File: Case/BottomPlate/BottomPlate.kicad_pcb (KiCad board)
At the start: 2 copper layers, 136.5 x 87.7 mm, 8 parts

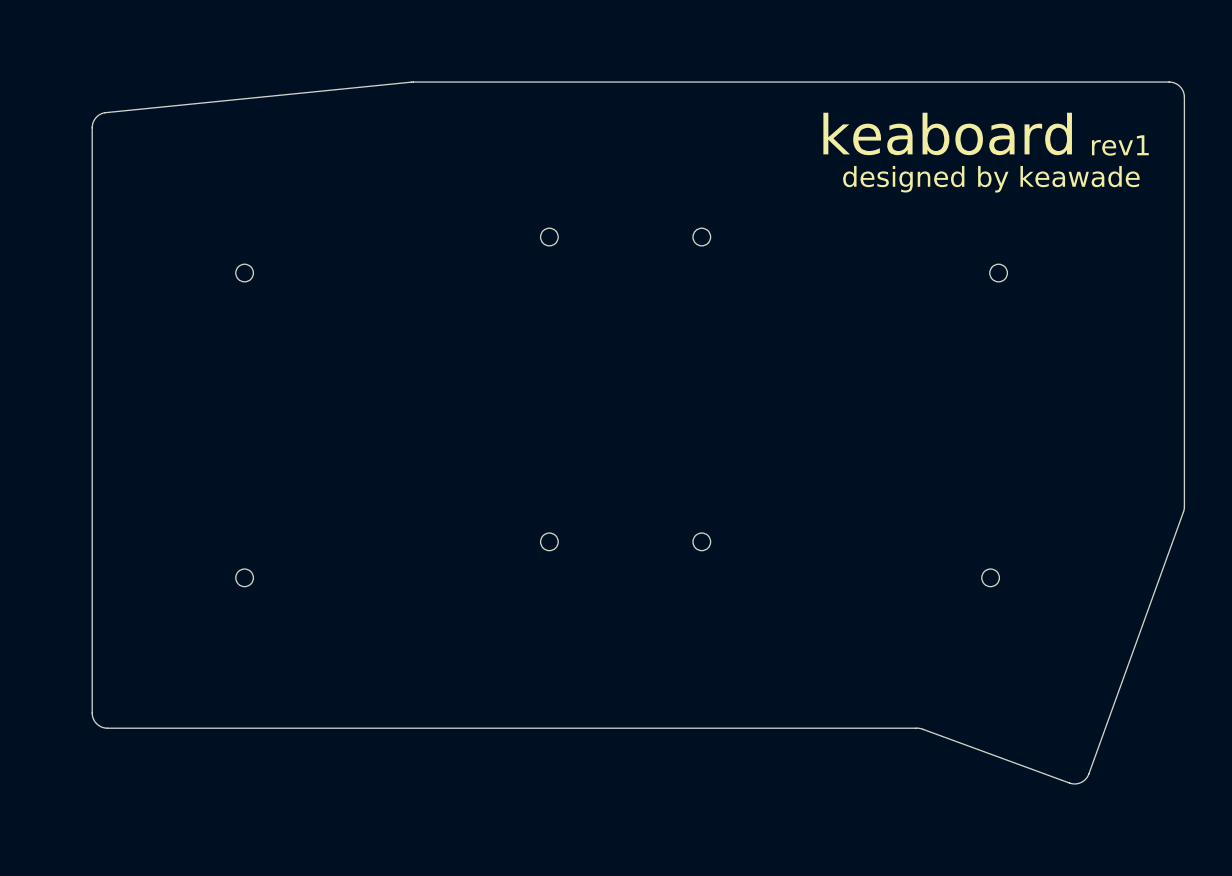
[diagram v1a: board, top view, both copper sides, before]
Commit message: Resize PCB to add more space around the edges to avoid breaking parts, update images, update gerber
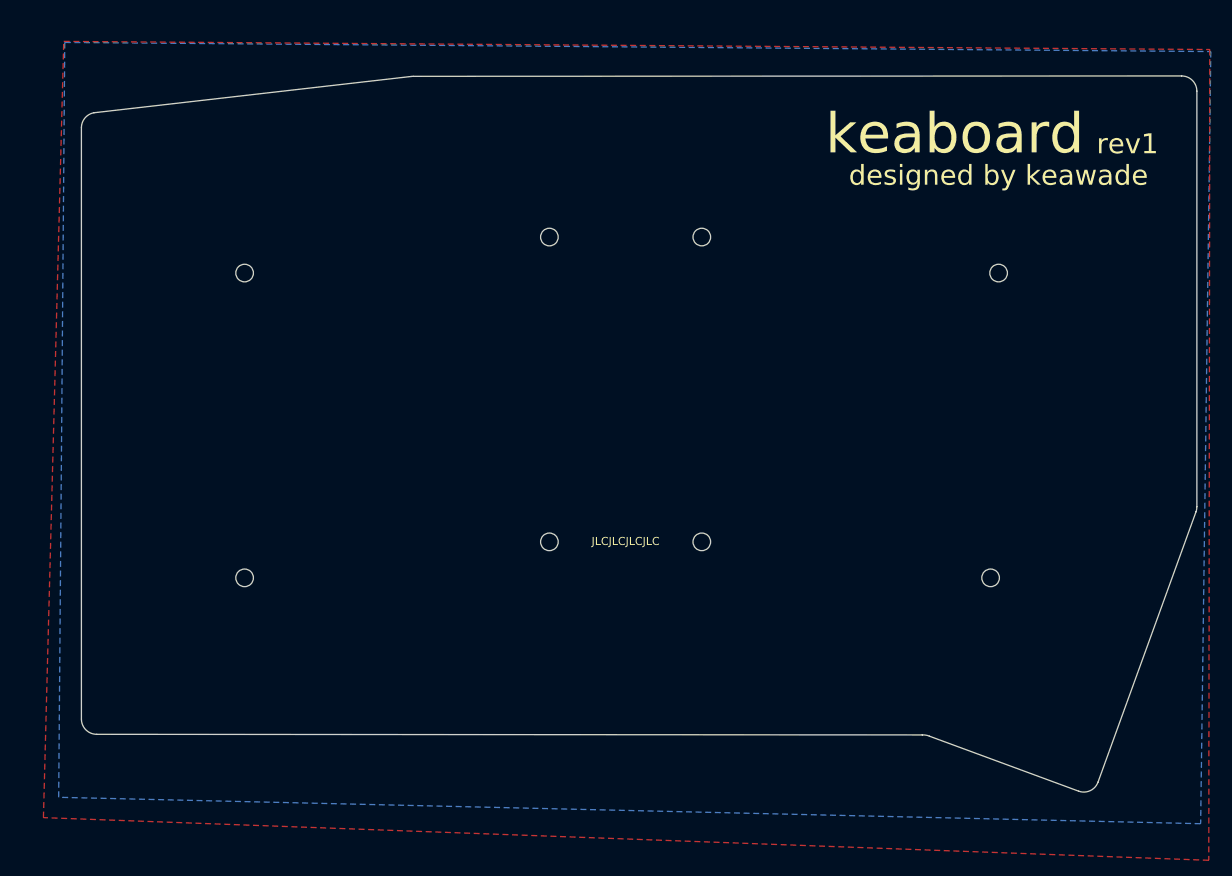
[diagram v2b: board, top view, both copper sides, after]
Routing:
- added copper zone on B.Cu, net (none)
- added copper zone on F.Cu, net (none)
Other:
- board size 136.5 x 87.7 mm -> 139.4 x 89.5 mm
- board text added: "JLCJLCJLCJLC"
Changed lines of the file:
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@@
   (general
     (thickness 1.6)
-    (drawings 20)
+    (drawings 21)
     (tracks 0)
     (zones 0)
@@
     (visible_elements FFFFFF7F)
     (pcbplotparams
-      (layerselection 0x010f0_ffffffff)
+      (layerselection 0x010fc_ffffffff)
       (usegerberextensions false)
       (usegerberattributes true)
@@
     (pad 1 np_thru_hole circle (at 0 0) (size 2.2 2.2) (drill 2.2) (layers *.Cu *.Mask))
   )
-  (gr_text keaboard (at 154.94 58.42) (layer B.SilkS)
+  (gr_text JLCJLCJLCJLC (at 114.681 103.759) (layer F.SilkS)
+    (effects (font (size 1 1) (thickness 0.2)))
+  )
+  (gr_arc (start 88.138 47.546) (end 88.138 45.641) (angle -7.594647344) (layer Edge.Cuts) (width 0.1))
+  (gr_line (start 48.2312 50.193941) (end 87.886228 45.657711) (layer Edge.Cuts) (width 0.1))
+  (gr_line (start 46.657 125.984) (end 46.657 52.07) (layer Edge.Cuts) (width 0.1))
+  (gr_arc (start 151.892001 129.898249) (end 152.654 128.12025) (angle -26.95486857) (layer Edge.Cuts) (width 0.1))
+  (gr_line (start 88.138 45.641) (end 184.186 45.593) (layer Edge.Cuts) (width 0.1))
+  (gr_line (start 185.98101 100.076) (end 173.735996 133.858) (layer Edge.Cuts) (width 0.1))
+  (gr_line (start 151.765273 127.968) (end 48.562 127.889) (layer Edge.Cuts) (width 0.1))
+  (gr_line (start 186.091 47.498) (end 186.091 99.441) (layer Edge.Cuts) (width 0.1))
+  (gr_arc (start 48.562 125.984) (end 46.657 125.984) (angle -90) (layer Edge.Cuts) (width 0.1))
+  (gr_arc (start 48.562 52.07) (end 46.657 52.07) (angle 80) (layer Edge.Cuts) (width 0.1))
+  (gr_arc (start 184.186 47.498) (end 186.091 47.498) (angle -90) (layer Edge.Cuts) (width 0.1))
+  (gr_line (start 171.323 135.001) (end 152.654 128.12025) (layer Edge.Cuts) (width 0.1))
+  (gr_arc (start 184.20301 99.441001) (end 185.98101 100.076) (angle -19.65382589) (layer Edge.Cuts) (width 0.1))
+  (gr_arc (start 171.957998 133.223002) (end 171.323 135.001) (angle -90) (layer Edge.Cuts) (width 0.1))
+  (gr_text keaboard (at 155.829 58.166) (layer B.SilkS)
     (effects (font (size 5 5) (thickness 0.75)) (justify mirror))
   )
-  (gr_text rev1 (at 176.53 57.15) (layer B.SilkS)
+  (gr_text rev1 (at 177.419 56.896) (layer B.SilkS)
     (effects (font (size 2.5 2.5) (thickness 0.4)) (justify mirror))
   )
-  (gr_text "designed by keawade" (at 160.401 53.213) (layer B.SilkS)
+  (gr_text "designed by keawade" (at 161.29 52.959) (layer B.SilkS)
     (effects (font (size 2.5 2.5) (thickness 0.4)) (justify mirror))
   )
-  (gr_text rev1 (at 176.53 54.356) (layer F.SilkS)
+  (gr_text rev1 (at 177.419 54.102) (layer F.SilkS)
     (effects (font (size 2.5 2.5) (thickness 0.4)))
   )
-  (gr_text keaboard (at 154.94 53.086) (layer F.SilkS)
+  (gr_text keaboard (at 155.829 52.832) (layer F.SilkS)
     (effects (font (size 5 5) (thickness 0.75)))
   )
-  (gr_text "designed by keawade" (at 160.401 58.293) (layer F.SilkS)
+  (gr_text "designed by keawade" (at 161.29 58.039) (layer F.SilkS)
     (effects (font (size 2.5 2.5) (thickness 0.4)))
   )
-  (gr_line (start 184.42101 100.076) (end 172.593 132.842) (layer Edge.Cuts) (width 0.1))
-  (gr_arc (start 88.138 48.26) (end 88.138 46.355) (angle -7.594647344) (layer Edge.Cuts) (width 0.1))
-  (gr_line (start 170.180002 133.984998) (end 151.891727 127.27925) (layer Edge.Cuts) (width 0.1))
-  (gr_line (start 49.5802 50.193941) (end 87.886228 46.371711) (layer Edge.Cuts) (width 0.1))
-  (gr_arc (start 151.129728 129.057249) (end 151.891727 127.27925) (angle -26.95486857) (layer Edge.Cuts) (width 0.1))
-  (gr_arc (start 49.911 125.222) (end 48.006 125.222) (angle -90) (layer Edge.Cuts) (width 0.1))
-  (gr_line (start 151.003 127.127) (end 49.911 127.127) (layer Edge.Cuts) (width 0.1))
-  (gr_line (start 48.006 125.222) (end 48.006 52.07) (layer Edge.Cuts) (width 0.1))
-  (gr_arc (start 182.626 48.26) (end 184.531 48.26) (angle -90) (layer Edge.Cuts) (width 0.1))
-  (gr_arc (start 170.815 132.207) (end 170.180002 133.984998) (angle -90) (layer Edge.Cuts) (width 0.1))
-  (gr_arc (start 49.911 52.07) (end 48.006 52.07) (angle 80) (layer Edge.Cuts) (width 0.1))
-  (gr_arc (start 182.64301 99.441001) (end 184.42101 100.076) (angle -19.65382589) (layer Edge.Cuts) (width 0.1))
-  (gr_line (start 184.531 48.26) (end 184.531 99.441) (layer Edge.Cuts) (width 0.1))
-  (gr_line (start 88.138 46.355001) (end 182.626 46.355) (layer Edge.Cuts) (width 0.1))
+  (zone (net 0) (net_name "") (layer F.Cu) (hatch edge 0.508)
+    (connect_pads (clearance 0.508))
+    (min_thickness 0.254)
+    (fill yes (arc_segments 32) (thermal_gap 0.508) (thermal_bridge_width 0.508))
+    (polygon
+      (pts
+        (xy 187.706 42.291) (xy 187.579 143.637) (xy 41.91 138.303) (xy 44.45 41.275)
+      )
+    )
+  )
+  (zone (net 0) (net_name "") (layer B.Cu) (hatch edge 0.508)
+    (connect_pads (clearance 0.508))
+    (min_thickness 0.254)
+    (fill yes (arc_segments 32) (thermal_gap 0.508) (thermal_bridge_width 0.508))
+    (polygon
+      (pts
+        (xy 187.833 42.545) (xy 186.563 139.065) (xy 43.815 135.763) (xy 44.577 41.402)
+      )
+    )
+  )
 )

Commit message: Update cases, update edge cuts on main pcb, start routing traces to controller
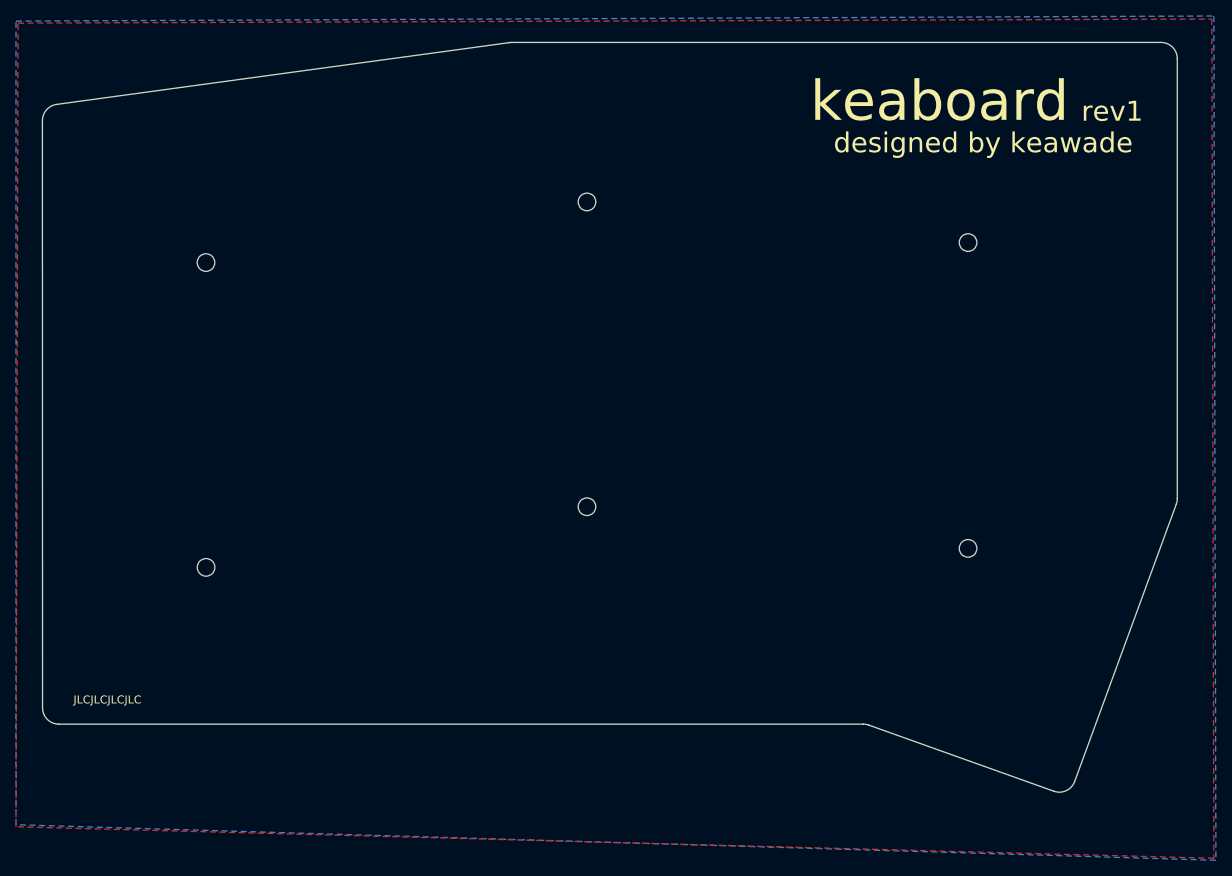
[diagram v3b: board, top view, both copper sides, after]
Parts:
- removed the REF** at (105.2, 65.7)
- removed the REF** at (160.3, 108.3)
- removed the REF** at (105.2, 103.8)
- removed the REF** at (161.3, 70.2)
- removed the REF** at (67.1, 108.3)
- removed the REF** at (67.1, 70.2)
- removed the REF** at (124.2, 65.7)
- removed the REF** at (124.2, 103.8)
- added REF**: MountingHole_2.2mm_M2, MountingHole:MountingHole_2.2mm_M2, F.Cu at (62.2, 68.9)
- added REF**: MountingHole_2.2mm_M2, MountingHole:MountingHole_2.2mm_M2, F.Cu at (62.2, 107.0)
- added REF**: MountingHole_2.2mm_M2, MountingHole:MountingHole_2.2mm_M2, F.Cu at (109.9, 99.4)
- added REF**: MountingHole_2.2mm_M2, MountingHole:MountingHole_2.2mm_M2, F.Cu at (109.9, 61.3)
- added REF**: MountingHole_2.2mm_M2, MountingHole:MountingHole_2.2mm_M2, F.Cu at (157.5, 104.6)
- added REF**: MountingHole_2.2mm_M2, MountingHole:MountingHole_2.2mm_M2, F.Cu at (157.5, 66.4)
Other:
- board size 139.4 x 89.5 mm -> 141.9 x 93.7 mm
